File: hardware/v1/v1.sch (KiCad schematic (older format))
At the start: 0 parts

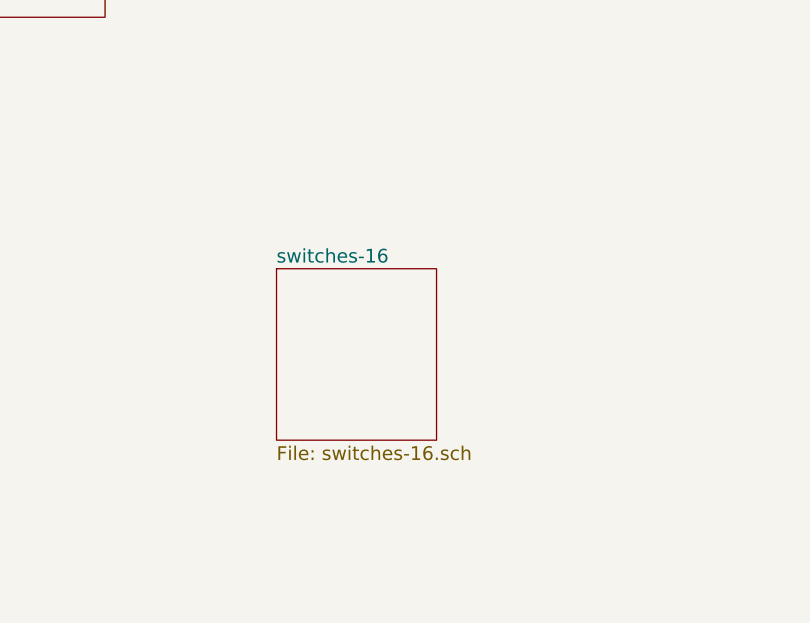
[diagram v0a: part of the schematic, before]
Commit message: Add keys-8 schematic and initial pcb layout file.
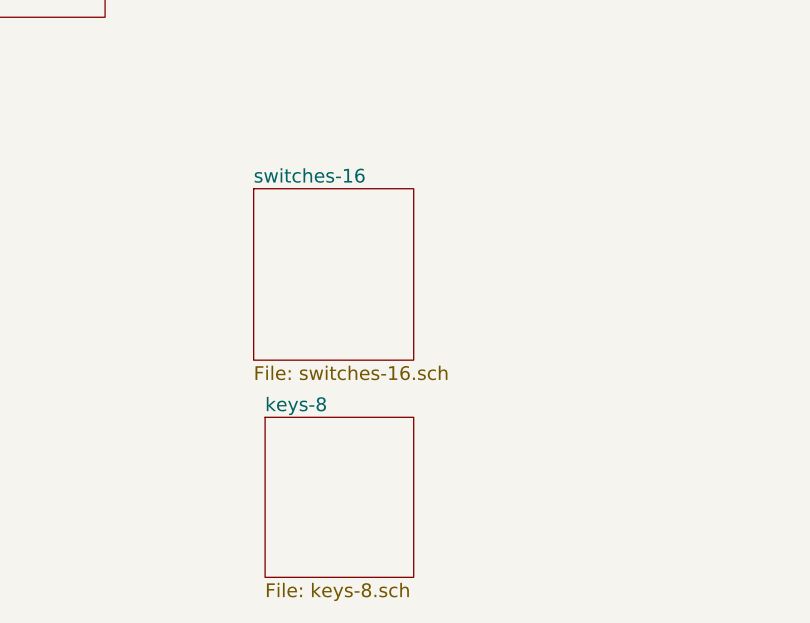
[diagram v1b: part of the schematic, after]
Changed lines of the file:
@@
 $Descr A4 11693 8268
 encoding utf-8
-Sheet 1 25
+Sheet 1 26
 Title ""
 Date ""
@@
 $EndSheet
 $Sheet
-S 3300 5000 700  750
+S 3200 4650 700  750
 U 57A4FF98
 F0 "switches-16" 60
 F1 "switches-16.sch" 60
 $EndSheet
+$Sheet
+S 3250 5650 650  700
+U 57A4B894
+F0 "keys-8" 60
+F1 "keys-8.sch" 60
+$EndSheet
 $EndSCHEMATC
